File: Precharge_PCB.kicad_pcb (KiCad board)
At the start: 2 copper layers, 180 x 100.4 mm, 168 parts, among them J1 Conn_01x02, J2 Conn_01x02, J3 Conn_01x02, J4 Conn_01x02, J5 Conn_01x08, J6 Conn_01x03, J7 Conn_01x04, J8 Conn_01x04, J9 Conn_01x06, K1 G2RL-1A, K2 G2RL-1A, K3 G9EJH-1-E, K4 SPU01L-05, Q1 DMN61D8LQ, Q2 DMN61D8LQ, Q3 DMN61D8LQ, Q4 DMN61D8LQ, Q5 DMN61D8LQ, Q6 DMN61D8LQ, Q7 DMN61D8LQ, Q8 DMN61D8LQ, SW1 SW_Push, U1 TPS7B88, U2 MCP1700x-330xxMB, U3 STM32F103C8Tx, U4 SN65HVD1050D, U5 LM393, U6 4N35, U7 AMC1351, U8 AMC1351, U9 TLV6002, Y1 8M

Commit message: *: Remove AIR flyback diodes
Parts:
- removed D19, D20: 1N4007, Diode_SMD:D_SMA
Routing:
- net SHUTDOWN_FINAL: track 227.7 -> 206.4 mm
- net Net-(J8-Pin_1): track 22.5 -> 11.9 mm
- net Net-(J7-Pin_1): track 22.5 -> 11.9 mm

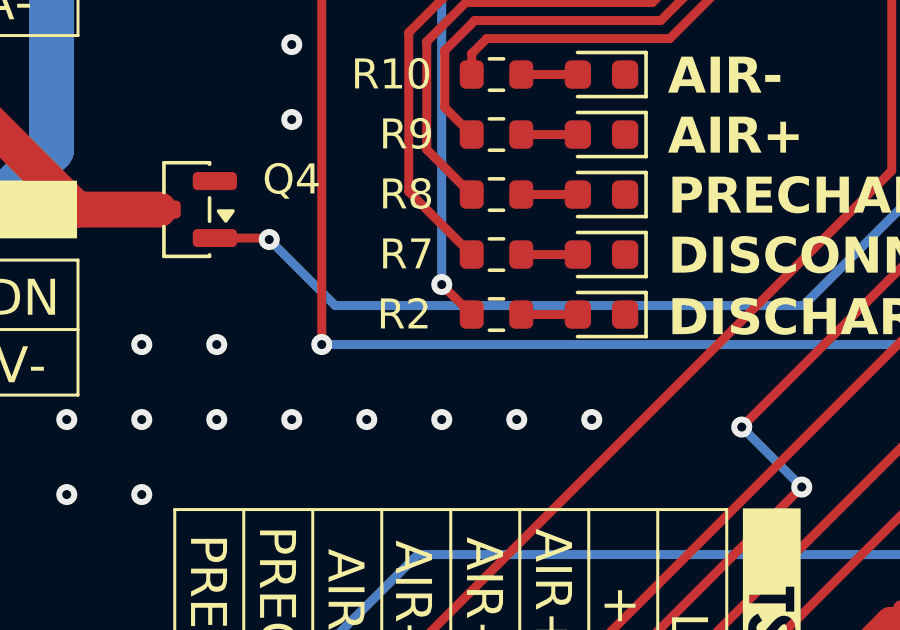
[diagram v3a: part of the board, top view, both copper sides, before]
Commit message: schematic: Group all STM LEDs together
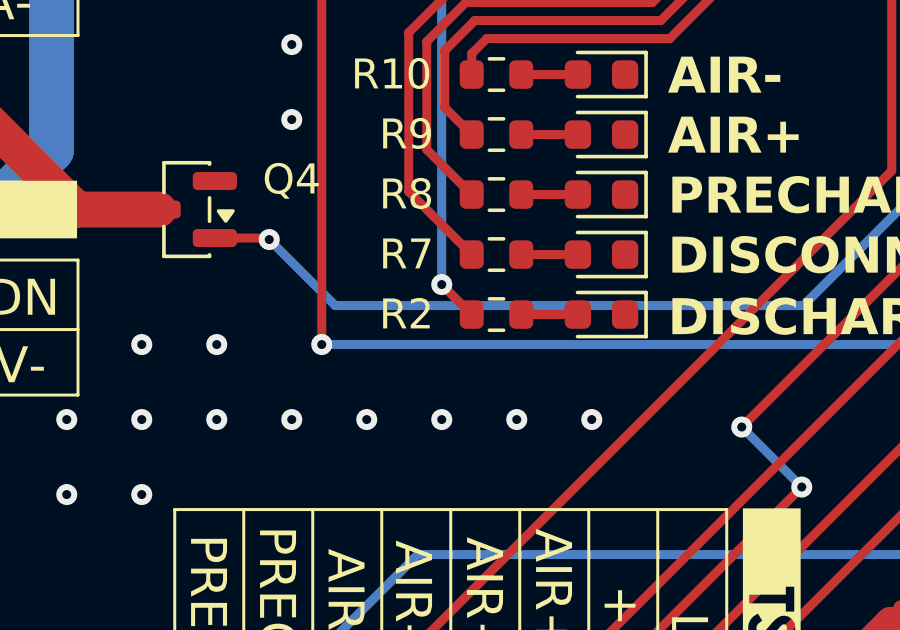
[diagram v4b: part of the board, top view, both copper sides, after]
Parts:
- turned R2 to 0 degrees
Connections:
- R2 pad 1: Net-(D6-A) -> Net-(U3-PB4)
- R2 pad 2: /STATUS LED -> Net-(D6-A)
- U3 pad 40: /STATUS LED -> Net-(U3-PB4)
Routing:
- net Net-(U3-PB4): track 0.00 -> 39.8 mm, vias 0 -> 2
- net /STATUS LED: track 39.8 -> 0.00 mm, vias 2 -> 0

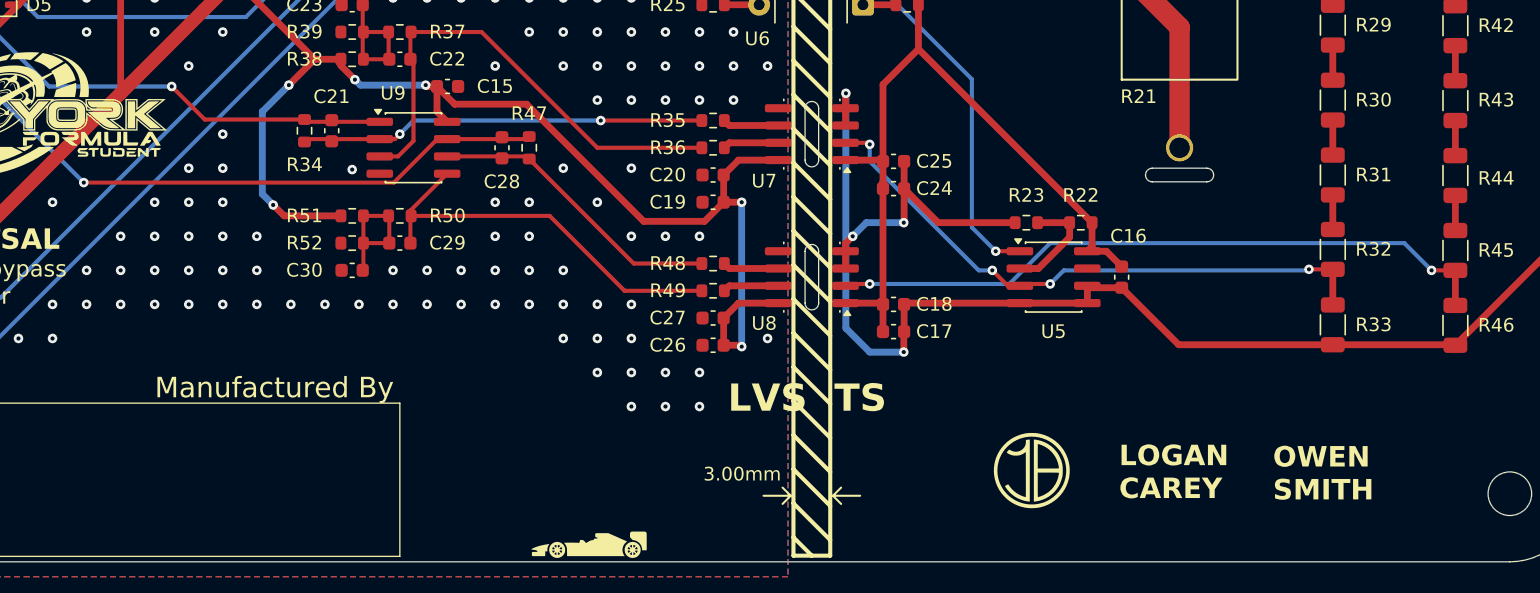
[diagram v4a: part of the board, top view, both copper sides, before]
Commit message: *: Add test points around sampling
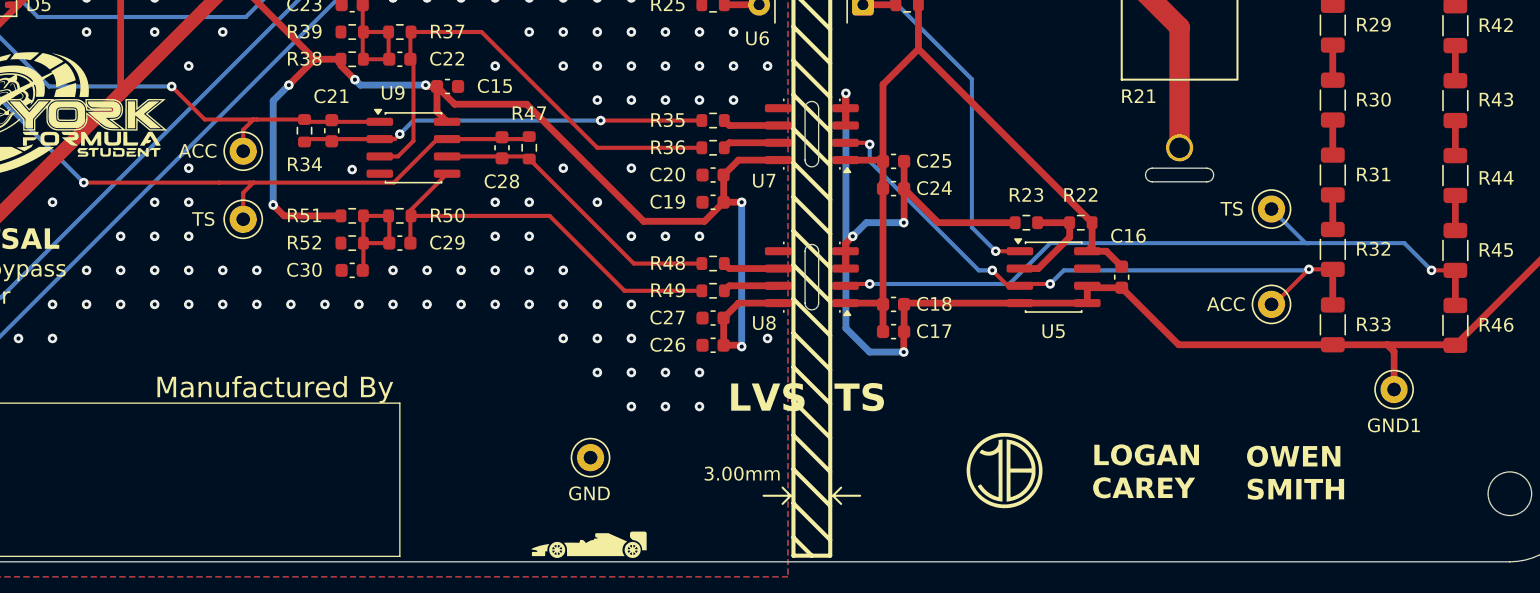
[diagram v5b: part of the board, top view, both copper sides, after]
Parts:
- added TP10: TestPoint, TestPoint:TestPoint_Keystone_5000-5004_Miniature, F.Cu at (139.0, 101.2)
- added TP11: TestPoint, TestPoint:TestPoint_Keystone_5000-5004_Miniature, F.Cu at (139.0, 106.2)
- added TP6: TestPoint, TestPoint:TestPoint_Keystone_5000-5004_Miniature, F.Cu at (164.5, 123.8)
- added TP7: TestPoint, TestPoint:TestPoint_Keystone_5000-5004_Miniature, F.Cu at (223.5, 118.8)
- added TP8: TestPoint, TestPoint:TestPoint_Keystone_5000-5004_Miniature, F.Cu at (214.5, 112.5)
- added TP9: TestPoint, TestPoint:TestPoint_Keystone_5000-5004_Miniature, F.Cu at (214.5, 105.5)
- moved G*** 2.00 mm to (194.9, 124.7)
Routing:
- net /HV Sampling/ACC Sampler/SCALED: track 44.0 -> 47.8 mm
- net /HV Sampling/TS Sampler/SCALED: track 49.5 -> 53.3 mm
- net GND1: track 249.7 -> 253.2 mm
- net /HV Sampling/Tractive System: track 83.4 -> 86.4 mm
- net /HV Sampling/Accumulator: track 67.5 -> 70.1 mm
- net +3V3: track 202.4 -> 201.7 mm
- net GND: vias 358 -> 353
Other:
- board text added: "ACC"
- board text added: "GND"
- board text added: "GND1"
